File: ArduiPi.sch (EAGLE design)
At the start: 95 parts, among them IC1 AVR-MEGA8-PPTH, IC2 DS2482-100S, J1 Teleinfo, J11 DNP, J12 DNP, J13 DNP, J2 DNP, J3 DNP, J4 DNP, J5 DNP, J6 DNP, J7 DNP, J8 DNP, J9 DC-044-AH, Q1 BSS138, Q2 BSS138, Q3 BSS138, Q4 BSS138, Q5 BSS84, U1 78M05, U2 LD1117 3V3, U3 TXB0104, U4 TXB0108, U5 TXB0108, X1 16Mhz

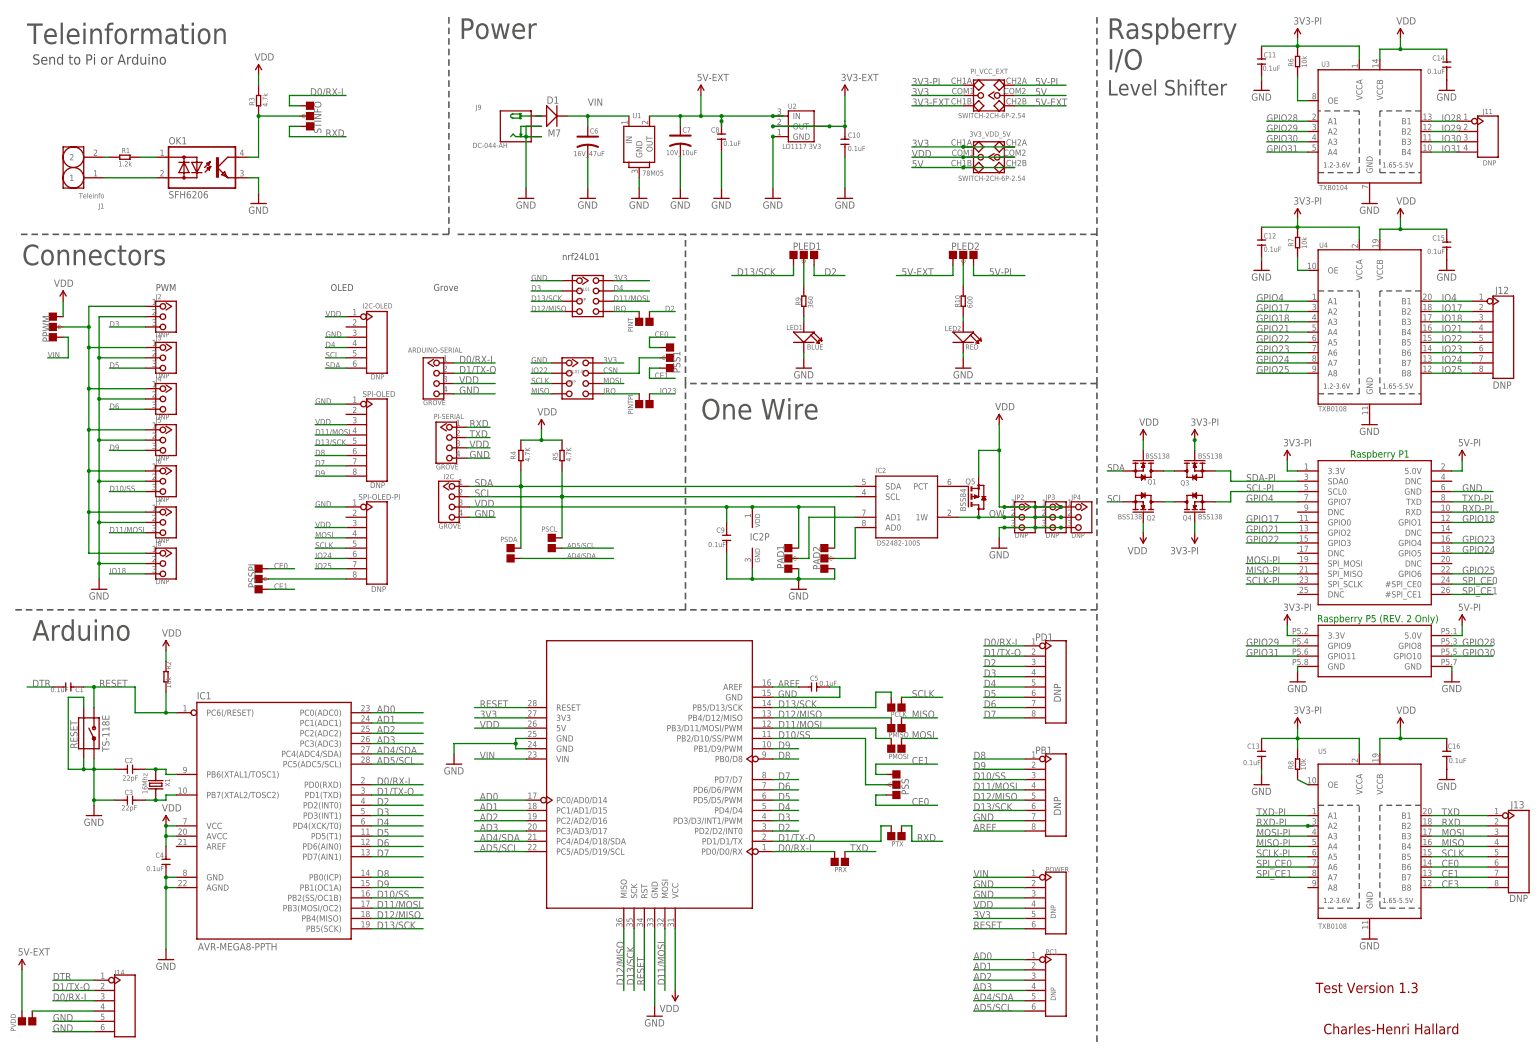
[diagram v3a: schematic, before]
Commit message: 2nd Prototype Board
2nd Version of the prototype board, near final version.

Changes :

- Removed R3 pullup from the output of the SFH6206
- Changed Level Shifting of RX line, now goes through 2 new FET
transistors Q7 and Q6 (BSS138 like I2C) and removed the connection of RX
from the TXB0108 (U5)
- Letting 2 TXB0108 of U5 ports free, I decided to bring them to
end users (if they need) putting 2 soldering pad JFREE1 and JFREE2 and
removed the pull down R12
- Changed soldering pad connection of TX/RX from Arduino to PI by
jumper because is we connect Arduino with Pi by serial, this will
conflict
during Arduino programming using FTDI cable. With jumpers we could
remove them during the firmware upload on the Arduino and put them back
after (much easier than solder/unsolder)
- Added a test led on PI I/O, because when I test program on PI I
do not have any indicator the program is working fine, so this led could
be
setup to blink in the program as visual test
- Added a new soldering pad to choose who drive the RST Line of I2C
OLED connector (I/O port of Pi or Arduino) letting user to choose what
will
drive this OLED by I2C (Pi or Arduino)
- Changed R10 and R11 value to 1K and R9 value to 470
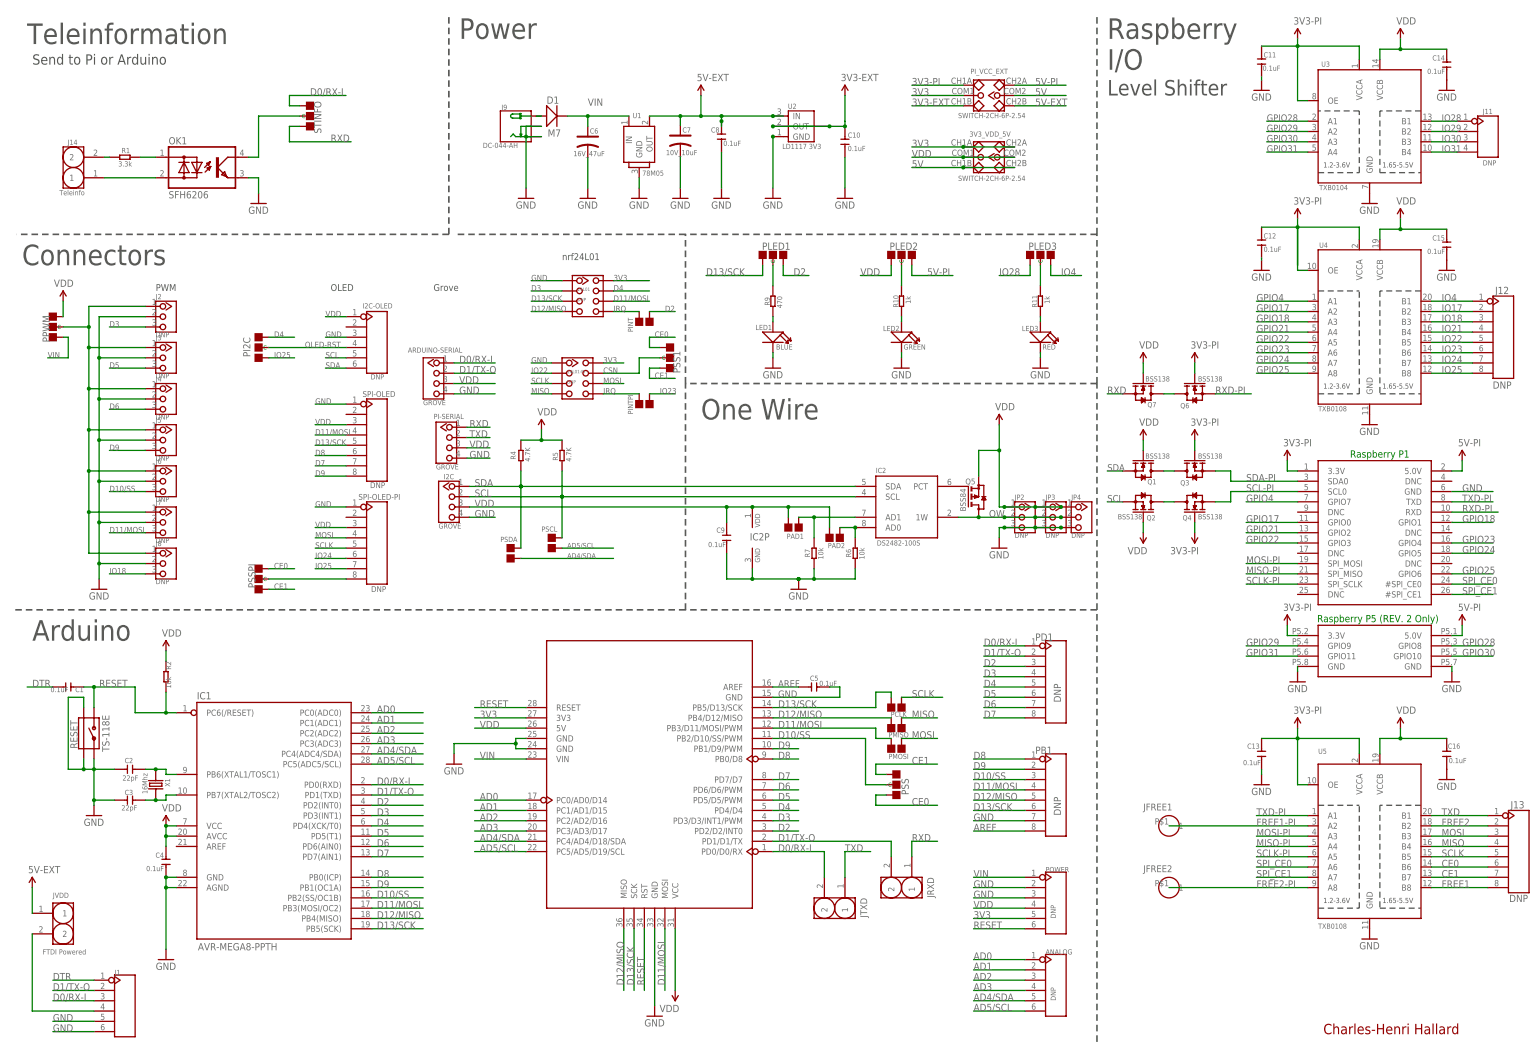
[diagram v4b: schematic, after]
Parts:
- removed PRX: PRX, Discrete:PAD-JUMPER-2P
- removed PTX: PTX, Discrete:PAD-JUMPER-2P
- removed PVDD: PVDD, Discrete:PAD-JUMPER-2P
- removed R3: 4.7k, Discrete:R-0603
- removed R8: 10k, Discrete:R-0603
- added JFREE1, JFREE2: (no value), Seeedstudio-Connector:HEADER-1P-32
- added JRXD: J2, Seeedstudio-Connector:HEADER-2P-2.54
- added JTXD: J1, Seeedstudio-Connector:HEADER-2P-2.54
- added JVDD: FTDI Powered, Seeedstudio-Connector:HEADER-2P-2.54
- added LED3: RED, Discrete:LED'0603'
- added PI2C, PLED3: (no value), Discrete:PAD-JUMPER-3P-40*40
- added Q6, Q7: BSS138, Seeedstudio-Discreter.rpt:MOSFET-N-SOT23
- added R11: 1k, Discrete:R-0603
- J1: value Teleinfo -> (none); device Seeedstudio-Connector:HEADER-2P-2.54 -> Connector:HEADER-6P-65/35MIL
- J14: value (none) -> Teleinfo; device Connector:HEADER-6P-65/35MIL -> Seeedstudio-Connector:HEADER-2P-2.54
- LED2: value RED -> GREEN
- PAD1: value (none) -> PAD1; device Discrete:PAD-JUMPER-3P-40*40 -> Discrete:PAD-JUMPER-2P
- PAD2: value (none) -> PAD2; device Discrete:PAD-JUMPER-3P-40*40 -> Discrete:PAD-JUMPER-2P
- R1: value 1.2k -> 3.3k
- R10: value 600 -> 1k
- R9: value 360 -> 470
- renumbered PC1 to ANALOG
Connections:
- net CE3 renamed FREE1
- new net FREE1-PI: JFREE1.1, U5.A2
- new net FREE2: J13.2, U5.B2
- new net FREE2-PI: JFREE2.1, U5.A8
- new net OLED-RST: I2C-OLED.4, PI2C.C
- net 3V3-PI: now also Q6.G, U3.OE, U4.OE, U5.OE; no longer R6.2, R7.2, R8.2
- net 5V-EXT: now also JVDD.1; no longer PLED2.L, PVDD.2
- net D0/RX-I: now also J1.3, JTXD.2; no longer J14.3, PRX.2
- net D1/TX-O: now also J1.2, JRXD.2; no longer J14.2, PTX.2
- net D4: now also PI2C.R; no longer I2C-OLED.4
- net DTR: now also J1.1; no longer J14.1
- net GND: now also J1.5, J1.6, LED3.-, R6.1, R7.1; no longer J14.5, J14.6, PAD1.L, PAD2.L
- net IO25: now also PI2C.L
- net IO28: now also PLED3.L
- net IO4: now also PLED3.R
- net N$1: no longer R3.1
- net N$10: now also J1.4, JVDD.2; no longer J14.4, PVDD.1
- net N$11: now also PAD1.1, R7.2; no longer PAD1.C
- net N$13: now also LED3.+, R11.2; no longer R8.1, U5.OE
- net N$14: now also J14.2; no longer J1.2
- net N$19: now also PLED3.C, R11.1; no longer R6.1, U3.OE
- net N$2: now also PAD2.1, R6.2; no longer PAD2.C
- net N$7: now also Q6.D, Q7.D; no longer R7.1, U4.OE
- net N$9: now also J14.1; no longer J1.1
- net RXD: now also JRXD.1, Q7.S; no longer J13.2, PTX.1, U5.B2
- net RXD-PI: now also Q6.S; no longer U5.A2
- net TXD: now also JTXD.1; no longer PRX.1
- net VDD: now also PAD1.2, PAD2.2, PLED2.L, Q7.G; no longer PAD1.R, PAD2.R, R3.2
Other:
- note removed: "Test Version 1.3"
- moved on the sheet: LED1, LED2, PLED1, PLED2, R10, R6, R7, R9

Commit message: ArduiPi Production Version V0.9d
ArduiPi Production Version V0.9d
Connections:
- net GPIO28: now also PI-P1.GPIO9; no longer PI-P1.GPIO8
- net GPIO29: now also PI-P1.GPIO8; no longer PI-P1.GPIO9
- net GPIO30: now also PI-P1.GPIO11; no longer PI-P1.GPIO10
- net GPIO31: now also PI-P1.GPIO10; no longer PI-P1.GPIO11
- net SCL: now also I2C.1; no longer I2C.2
- net SDA: now also I2C.2; no longer I2C.1
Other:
- moved on the sheet: J11
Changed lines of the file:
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@@
 <?xml version="1.0" encoding="utf-8"?>
 <!DOCTYPE eagle SYSTEM "eagle.dtd">
-<eagle version="6.3">
+<eagle version="6.4">
 <drawing>
 <settings>
@@
 <setting verticaltext="up"/>
 </settings>
-<grid distance="0.1" unitdist="inch" unit="inch" style="lines" multiple="1" display="no" altdistance="0.01" altunitdist="inch" altunit="inch"/>
+<grid distance="50" unitdist="mil" unit="mil" style="lines" multiple="1" display="yes" altdistance="25" altunitdist="mil" altunit="mil"/>
 <layers>
 <layer number="1" name="Top" color="4" fill="1" visible="no" active="no"/>
@@
 </instance>
 <instance part="GND26" gate="1" x="363.22" y="172.72"/>
-<instance part="J11" gate="G$1" x="392.43" y="189.23" smashed="yes">
-<attribute name="NAME" x="391.16" y="194.818" size="1.27" layer="95"/>
-<attribute name="VALUE" x="391.16" y="182.118" size="1.27" layer="96"/>
+<instance part="J11" gate="G$1" x="396.24" y="189.23" smashed="yes">
+<attribute name="NAME" x="394.97" y="194.818" size="1.27" layer="95"/>
+<attribute name="VALUE" x="394.97" y="182.118" size="1.27" layer="96"/>
 </instance>
 <instance part="Q5" gate="G$1" x="266.7" y="100.33" smashed="yes">
@@
 <segment>
 <pinref part="IC2" gate="G$1" pin="SCL"/>
-<label x="142.24" y="100.33" size="1.778" layer="95"/>
-<pinref part="I2C" gate="G$1" pin="2"/>
+<label x="142.24" y="102.87" size="1.778" layer="95"/>
 <pinref part="PSCL" gate="G$1" pin="2"/>
 <wire x1="236.22" y1="100.33" x2="163.83" y2="100.33" width="0.1524" layer="91"/>
-<wire x1="163.83" y1="100.33" x2="140.97" y2="100.33" width="0.1524" layer="91"/>
 <wire x1="163.83" y1="90.17" x2="163.83" y2="100.33" width="0.1524" layer="91"/>
 <junction x="163.83" y="100.33"/>
 <junction x="163.83" y="100.33"/>
-<wire x1="163.83" y1="106.68" x2="163.83" y2="100.33" width="0.1524" layer="91"/>
+<wire x1="163.83" y1="106.68" x2="163.83" y2="104.14" width="0.1524" layer="91"/>
 <pinref part="R5" gate="R" pin="1"/>
+<pinref part="I2C" gate="G$1" pin="1"/>
+<wire x1="163.83" y1="104.14" x2="163.83" y2="100.33" width="0.1524" layer="91"/>
+<wire x1="140.97" y1="102.87" x2="152.4" y2="102.87" width="0.1524" layer="91"/>
+<wire x1="152.4" y1="102.87" x2="152.4" y2="104.14" width="0.1524" layer="91"/>
+<wire x1="152.4" y1="104.14" x2="153.67" y2="105.41" width="0.1524" layer="91" curve="-90"/>
+<wire x1="153.67" y1="105.41" x2="154.94" y2="104.14" width="0.1524" layer="91" curve="-90"/>
+<wire x1="154.94" y1="104.14" x2="163.83" y2="104.14" width="0.1524" layer="91"/>
+<junction x="163.83" y="104.14"/>
 </segment>
 <segment>
@@
 <segment>
 <pinref part="IC2" gate="G$1" pin="SDA"/>
-<label x="142.24" y="102.87" size="1.778" layer="95"/>
-<pinref part="I2C" gate="G$1" pin="1"/>
+<label x="142.24" y="100.33" size="1.778" layer="95"/>
 <pinref part="PSDA" gate="G$1" pin="2"/>
 <wire x1="236.22" y1="102.87" x2="153.67" y2="102.87" width="0.1524" layer="91"/>
-<wire x1="153.67" y1="102.87" x2="140.97" y2="102.87" width="0.1524" layer="91"/>
-<wire x1="153.67" y1="87.63" x2="153.67" y2="102.87" width="0.1524" layer="91"/>
+<wire x1="153.67" y1="87.63" x2="153.67" y2="100.33" width="0.1524" layer="91"/>
 <junction x="153.67" y="102.87"/>
 <junction x="153.67" y="102.87"/>
+<wire x1="153.67" y1="100.33" x2="153.67" y2="102.87" width="0.1524" layer="91"/>
 <wire x1="153.67" y1="106.68" x2="153.67" y2="102.87" width="0.1524" layer="91"/>
 <pinref part="R4" gate="R" pin="1"/>
+<pinref part="I2C" gate="G$1" pin="2"/>
+<wire x1="140.97" y1="100.33" x2="153.67" y2="100.33" width="0.1524" layer="91"/>
+<junction x="153.67" y="100.33"/>
 </segment>
 <segment>
@@
 <net name="GPIO28" class="0">
 <segment>
+<pinref part="U3" gate="G$1" pin="A1"/>
+<wire x1="347.98" y1="193.04" x2="337.82" y2="193.04" width="0.1524" layer="91"/>
+<label x="337.82" y="193.04" size="1.6764" layer="95"/>
+</segment>
+<segment>
+<wire x1="345.44" y1="63.5" x2="332.74" y2="63.5" width="0.1524" layer="91"/>
+<label x="332.74" y="63.5" size="1.778" layer="95"/>
+<pinref part="PI-P1" gate="G$1" pin="GPIO9"/>
+</segment>
+</net>
+<net name="GPIO30" class="0">
+<segment>
+<pinref part="U3" gate="G$1" pin="A3"/>
+<wire x1="347.98" y1="187.96" x2="337.82" y2="187.96" width="0.1524" layer="91"/>
+<label x="337.82" y="187.96" size="1.6764" layer="95"/>
+</segment>
+<segment>
+<wire x1="345.44" y1="60.96" x2="332.74" y2="60.96" width="0.1524" layer="91"/>
+<label x="332.74" y="60.96" size="1.778" layer="95"/>
+<pinref part="PI-P1" gate="G$1" pin="GPIO11"/>
+</segment>
+</net>
+<net name="GPIO29" class="0">
+<segment>
+<pinref part="U3" gate="G$1" pin="A2"/>
+<wire x1="347.98" y1="190.5" x2="337.82" y2="190.5" width="0.1524" layer="91"/>
+<label x="337.82" y="190.5" size="1.6764" layer="95"/>
+</segment>
+<segment>
 <wire x1="383.54" y1="63.5" x2="393.7" y2="63.5" width="0.1524" layer="91"/>
 <label x="386.08" y="63.5" size="1.778" layer="95"/>
 <pinref part="PI-P1" gate="G$1" pin="GPIO8"/>
 </segment>
-<segment>
-<pinref part="U3" gate="G$1" pin="A1"/>
-<wire x1="347.98" y1="193.04" x2="337.82" y2="193.04" width="0.1524" layer="91"/>
-<label x="337.82" y="193.04" size="1.6764" layer="95"/>
-</segment>
-</net>
-<net name="GPIO30" class="0">
+</net>
+<net name="GPIO31" class="0">
+<segment>
+<pinref part="U3" gate="G$1" pin="A4"/>
+<wire x1="347.98" y1="185.42" x2="337.82" y2="185.42" width="0.1524" layer="91"/>
+<label x="337.82" y="185.42" size="1.6764" layer="95"/>
+</segment>
 <segment>
 <wire x1="383.54" y1="60.96" x2="393.7" y2="60.96" width="0.1524" layer="91"/>
 <label x="386.08" y="60.96" size="1.778" layer="95"/>
 <pinref part="PI-P1" gate="G$1" pin="GPIO10"/>
-</segment>
-<segment>
-<pinref part="U3" gate="G$1" pin="A3"/>
-<wire x1="347.98" y1="187.96" x2="337.82" y2="187.96" width="0.1524" layer="91"/>
-<label x="337.82" y="187.96" size="1.6764" layer="95"/>
-</segment>
-</net>
-<net name="GPIO29" class="0">
-<segment>
-<wire x1="345.44" y1="63.5" x2="332.74" y2="63.5" width="0.1524" layer="91"/>
-<label x="332.74" y="63.5" size="1.778" layer="95"/>
-<pinref part="PI-P1" gate="G$1" pin="GPIO9"/>
-</segment>
-<segment>
-<pinref part="U3" gate="G$1" pin="A2"/>
-<wire x1="347.98" y1="190.5" x2="337.82" y2="190.5" width="0.1524" layer="91"/>
-<label x="337.82" y="190.5" size="1.6764" layer="95"/>
-</segment>
-</net>
-<net name="GPIO31" class="0">
-<segment>
-<wire x1="345.44" y1="60.96" x2="332.74" y2="60.96" width="0.1524" layer="91"/>
-<label x="332.74" y="60.96" size="1.778" layer="95"/>
-<pinref part="PI-P1" gate="G$1" pin="GPIO11"/>
-</segment>
-<segment>
-<pinref part="U3" gate="G$1" pin="A4"/>
-<wire x1="347.98" y1="185.42" x2="337.82" y2="185.42" width="0.1524" layer="91"/>
-<label x="337.82" y="185.42" size="1.6764" layer="95"/>
 </segment>
 </net>
@@
 <segment>
 <pinref part="U3" gate="G$1" pin="B1"/>
-<wire x1="378.46" y1="193.04" x2="384.81" y2="193.04" width="0.1524" layer="91"/>
+<wire x1="378.46" y1="193.04" x2="388.62" y2="193.04" width="0.1524" layer="91"/>
 <label x="381" y="193.04" size="1.6764" layer="95"/>
 <pinref part="J11" gate="G$1" pin="P$1"/>
@@
 <segment>
 <pinref part="U3" gate="G$1" pin="B2"/>
-<wire x1="384.81" y1="190.5" x2="378.46" y2="190.5" width="0.1524" layer="91"/>
+<wire x1="388.62" y1="190.5" x2="378.46" y2="190.5" width="0.1524" layer="91"/>
 <label x="381" y="190.5" size="1.6764" layer="95"/>
 <pinref part="J11" gate="G$1" pin="P$2"/>
@@
 <segment>
 <pinref part="U3" gate="G$1" pin="B3"/>
-<wire x1="384.81" y1="187.96" x2="378.46" y2="187.96" width="0.1524" layer="91"/>
+<wire x1="388.62" y1="187.96" x2="378.46" y2="187.96" width="0.1524" layer="91"/>
 <label x="381" y="187.96" size="1.6764" layer="95"/>
 <pinref part="J11" gate="G$1" pin="P$3"/>
@@
 <segment>
 <pinref part="U3" gate="G$1" pin="B4"/>
-<wire x1="384.81" y1="185.42" x2="378.46" y2="185.42" width="0.1524" layer="91"/>
+<wire x1="388.62" y1="185.42" x2="378.46" y2="185.42" width="0.1524" layer="91"/>
 <label x="381" y="185.42" size="1.6764" layer="95"/>
 <pinref part="J11" gate="G$1" pin="P$4"/>
